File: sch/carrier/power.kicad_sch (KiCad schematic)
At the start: 0 parts

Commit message: noice.
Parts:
- added J1: 1054500101, MOLEXC:Molex-1054500101-MFG, symbol MOLEXC:1054500101
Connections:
- new net GND: J1.1 (MNT_1), J1.2 (MNT_2), J1.3 (MNT_3), J1.4 (MNT_4), J1.A1 (GND), J1.A12 (GND), J1.B1 (GND), J1.B12 (GND)

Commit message: goodnight
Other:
- title: (none) -> Power and battery
- moved on the sheet: J1A, J1B, J1C

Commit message: hhhhhhhhhhhhhhhhh
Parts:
- added D2: 5.1v, Diode_THT:D_DO-41_SOD81_P7.62mm_Horizontal, symbol Device:D_Zener
- added Q1, Q2: BC557, Package_TO_SOT_THT:TO-92_Inline, symbol Transistor_BJT:BC557
- added R14, R15: 5.1k, Resistor_SMD:R_0805_2012Metric_Pad1.20x1.40mm_HandSolder, symbol Device:R
- added R16: 2k, Resistor_SMD:R_0805_2012Metric_Pad1.20x1.40mm_HandSolder, symbol Device:R
- added R17: 1k, Resistor_SMD:R_0805_2012Metric_Pad1.20x1.40mm_HandSolder, symbol Device:R
- added R18: 6.2k, Resistor_SMD:R_0805_2012Metric_Pad1.20x1.40mm_HandSolder, symbol Device:R
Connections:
- net GND: now also D2.2 (A), R14.2, R15.2, R18.1
- net at J1.B4 (VBUS): now also J1.A4 (VBUS), J1.A9 (VBUS), J1.B9 (VBUS), Q1.1 (C), Q2.1 (C), R16.1
- net at J1.B5 (CC2): now also R15.1
- net at J1.A5 (CC1): now also R14.1
- new net: D2.1 (K), R16.2, R17.1
- new net: Q1.2 (B), R17.2
- new net: Q1.3 (E), Q2.2 (B), R18.2
- new net 5v: Q2.3 (E)
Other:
- note added: "5V 3A OUTPUT"
- note added: "5v overvolt prot - turns off >5.5v"

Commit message: put some stuff on the pcb - it is going to kill me trying to get all on
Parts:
- Q1, Q2: footprint Package_TO_SOT_THT:TO-92_Inline -> Package_TO_SOT_THT:TO-92_Inline_Horizontal1
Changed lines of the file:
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@@
-    (stroke (width 0) (type solid) (color 0 0 0 0))
-  )
-  (wire (pts (xy 66.675 142.875) (xy 85.725 142.875))
     (stroke (width 0) (type solid) (color 0 0 0 0))
   )
@@
     (effects (font (size 1.27 1.27)) (justify right bottom))
   )
-  (text "5v overvolt prot - turns off >5.5v\n" (at 96.52 107.315 180)
+  (text "5v overvolt prot - turns off >5.5v\n" (at 100.33 112.395 180)
     (effects (font (size 1.27 1.27)) (justify right bottom))
   )
-  (hierarchical_label "5v" (shape input) (at 107.95 139.065 0)
+  (hierarchical_label "5v" (shape output) (at 107.95 139.065 0)
     (effects (font (size 1.27 1.27)) (justify left))
   )
@@
     )
     (property "Datasheet" "" (id 3) (at 66.675 142.875 0)
+      (effects (font (size 1.27 1.27)) hide)
+    )
+    (pin "1")
+  )
+  (symbol (lib_id "power:GND") (at 85.725 142.875 0) (unit 1)
+    (in_bom yes) (on_board yes) (fields_autoplaced)
+    (property "Reference" "#PWR0101" (id 0) (at 85.725 149.225 0)
+      (effects (font (size 1.27 1.27)) hide)
+    )
+    (property "Value" "GND" (id 1) (at 85.725 147.32 0))
+    (property "Footprint" "" (id 2) (at 85.725 142.875 0)
+      (effects (font (size 1.27 1.27)) hide)
+    )
+    (property "Datasheet" "" (id 3) (at 85.725 142.875 0)
       (effects (font (size 1.27 1.27)) hide)
     )
@@
   )
   (symbol (lib_id "Device:D_Zener") (at 66.675 139.065 270) (unit 1)
-    (in_bom yes) (on_board yes) (fields_autoplaced)
+    (in_bom yes) (on_board yes)
     (property "Reference" "D2" (id 0) (at 69.215 137.7949 90)
       (effects (font (size 1.27 1.27)) (justify left))
@@
       (effects (font (size 1.27 1.27)) hide)
     )
-    (property "Model" "1N4733" (id 4) (at 66.675 139.065 90)
-      (effects (font (size 1.27 1.27)) hide)
-    )
+    (property "Model" "1N4733" (id 4) (at 61.595 139.065 90))
     (pin "1")
     (pin "2")
@@
       (effects (font (size 1.27 1.27)) (justify left))
     )
-    (property "Footprint" "Package_TO_SOT_THT:TO-92_Inline" (id 2) (at 88.265 129.54 0)
+    (property "Footprint" "Package_TO_SOT_THT:TO-92_Inline_Horizontal1" (id 2) (at 88.265 129.54 0)
       (effects (font (size 1.27 1.27) italic) (justify left) hide)
     )
@@
       (effects (font (size 1.27 1.27)) (justify left))
     )
-    (property "Footprint" "Package_TO_SOT_THT:TO-92_Inline" (id 2) (at 104.14 135.89 0)
+    (property "Footprint" "Package_TO_SOT_THT:TO-92_Inline_Horizontal1" (id 2) (at 104.14 135.89 0)
       (effects (font (size 1.27 1.27) italic) (justify left) hide)
     )
@@
   (symbol (lib_id "MOLEXC:1054500101") (at 28.575 52.705 0) (unit 1)
     (in_bom yes) (on_board yes)
-    (property "Reference" "J1" (id 0) (at 17.78 19.2405 90))
+    (property "Reference" "J1" (id 0) (at 19.05 42.7355 0))
     (property "Value" "1054500101" (id 1) (at 19.8755 44.45 0))
     (property "Footprint" "MOLEXC:Molex-1054500101-MFG" (id 2) (at 28.575 40.005 0)

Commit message: holy shit i hate chargers
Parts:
- added C? (x2): 4.7uF, symbol Device:C
- added C?: 10uF, symbol Device:C
- added R?: 110k, symbol Device:R
- added R?: 290k, symbol Device:R
- added U?: DS2745U, Package_SO:TSSOP-8_3x3mm_P0.65mm, symbol Battery_Management:DS2745U
- added U?: MCP73871-2CC, Package_DFN_QFN:QFN-20-1EP_4x4mm_P0.5mm_EP2.5x2.5mm, symbol Battery_Management:MCP73871-2CC
- added U?: MT3608, Package_TO_SOT_SMD:SOT-23-6, symbol Regulator_Switching:MT3608
- added U?: TPS61230DRC, Package_SON:Texas_S-PVSON-N10_ThermalVias, symbol Regulator_Switching:TPS61230DRC
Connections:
- net 5v: no longer Q2.3 (E)
- net GND: now also J1.A1 (GND), J1.A1 (GND), J1.A12 (GND), J1.A2 (TX1+), J1.A3 (TX1-), J1.A4 (VBUS), C?.2, C?.2, R?.2, U?.10 (VSS), U?.11 (VSS), U?.21 (VSS); no longer J1.1 (MNT_1), J1.2 (MNT_2), J1.3 (MNT_3), J1.4 (MNT_4), J1.B1 (GND), J1.B12 (GND)
- net at R15.1: now also J1.A5 (CC1); no longer J1.B5 (CC2)
- net at Q2.2 (B), R18.2: now also Q1.1 (C); no longer Q1.3 (E)
- new net: J1.A4 (VBUS), J1.A4 (VBUS), J1.A9 (VBUS), J1.A9 (VBUS), Q1.3 (E), Q2.3 (E), R16.1
- new net: R?.1, R?.2, U?.2 (VPCC)
- new net: C?.1, U?.14 (VBAT), U?.15 (VBAT), U?.16 (Vbat_SENSE)
- new net: C?.1, U?.1 (OUT), U?.20 (OUT)
- new net: U?.1 (SW), U?.2 (SW)
- new net: U?.3 (VOUT), U?.4 (VOUT)
- new net VUSB: C?.1, Q2.1 (C), R?.1, U?.18 (IN), U?.19 (IN)
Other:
- note added: "battery monitor board"

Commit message: h
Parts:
- removed C? (x2): 4.7uF, symbol Device:C
- removed C?: 10uF, symbol Device:C
- removed J1 (x3): 1054500101, MOLEXC:Molex-1054500101-MFG, symbol MOLEXC:1054500101
- removed R14, R15: 5.1k, Resistor_SMD:R_0805_2012Metric_Pad1.20x1.40mm_HandSolder, symbol Device:R
- removed R?: 110k, symbol Device:R
- removed R?: 290k, symbol Device:R
- removed U?: DS2745U, Package_SO:TSSOP-8_3x3mm_P0.65mm, symbol Battery_Management:DS2745U
- removed U?: MCP73871-2CC, Package_DFN_QFN:QFN-20-1EP_4x4mm_P0.5mm_EP2.5x2.5mm, symbol Battery_Management:MCP73871-2CC
- removed U?: MT3608, Package_TO_SOT_SMD:SOT-23-6, symbol Regulator_Switching:MT3608
- added C? (x5): C, symbol Device:C
- added D? (x2): LED, symbol Device:LED
- added J4: USB_C_Receptacle_USB2.0, Connector_USB:USB_C_Receptacle_JAE_DX07S016JA1R1500, symbol Connector:USB_C_Receptacle_USB2.0
- added L?: L, symbol Device:L
- added R20, R21: 5.1k, Resistor_SMD:R_0805_2012Metric_Pad1.20x1.40mm_HandSolder, symbol Device:R
- added R? (x8): R, symbol Device:R
- added R?: 0, symbol Device:R
- added U?: MP2617BGL-P, symbol MP:MP2617BGL-P
- gave numbers to parts that had none: 1
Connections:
- net GND: now also C?.1, C?.1, C?.2, J4.A1 (GND), J4.A12 (GND), J4.B1 (GND), J4.B12 (GND), R20.2, R21.2, R?.2, R?.2, R?.2, R?.2, U?.5 (PGND)
- new net: C?.2, L?.1, U?.13 (SYS)
- new net: J4.A5 (CC1), R20.1
- new net: D?.1 (K), U?.10 (*ACOK)
- new net: D?.2 (A), R?.1 (x2)
- new net: J4.B5 (CC2), R21.1
- new net: J4.S1 (SHIELD), R?.1
- new net: C?.2, R?.1
- new net: R?.1, U?.17 (ILIM)
- new net: R?.1, R?.2, U?.16 (NTC)
- new net: D?.1 (K), U?.9 (*CHGOK)
- new net: R?.1, U?.15 (ISET)
- new net: C?.1, L?.2, U?.2 (SW), U?.4 (SW)
- new net: C?.2, U?.1 (BST)
- new net: C?.2, U?.18 (TMR)
- new net BATT_CHRG: U?.14 (BATT)
- new net MP2617__vcc: R?.1, R?.1, R?.2, R?.2, R?.2, U?.19 (VLIM), U?.20 (VCC)
- new net VBUS: C?.1, J4.A4 (VBUS), J4.A9 (VBUS), J4.B4 (VBUS), J4.B9 (VBUS), R?.2
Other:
- note added: "Based off MP2617 datasheet. TODO: make the values do things."
- note added: "Too many people on stack overflow/exchange seem to be unable to agree on this! Leaving this unconnected with a 0 ohm so we can if we choose to."
- note added: "battery monitor board we will write software for this, but it is not intially required"
- note removed: "battery monitor board"
- moved on the sheet: D2, Q1, Q2, R16, R17, R18, U5

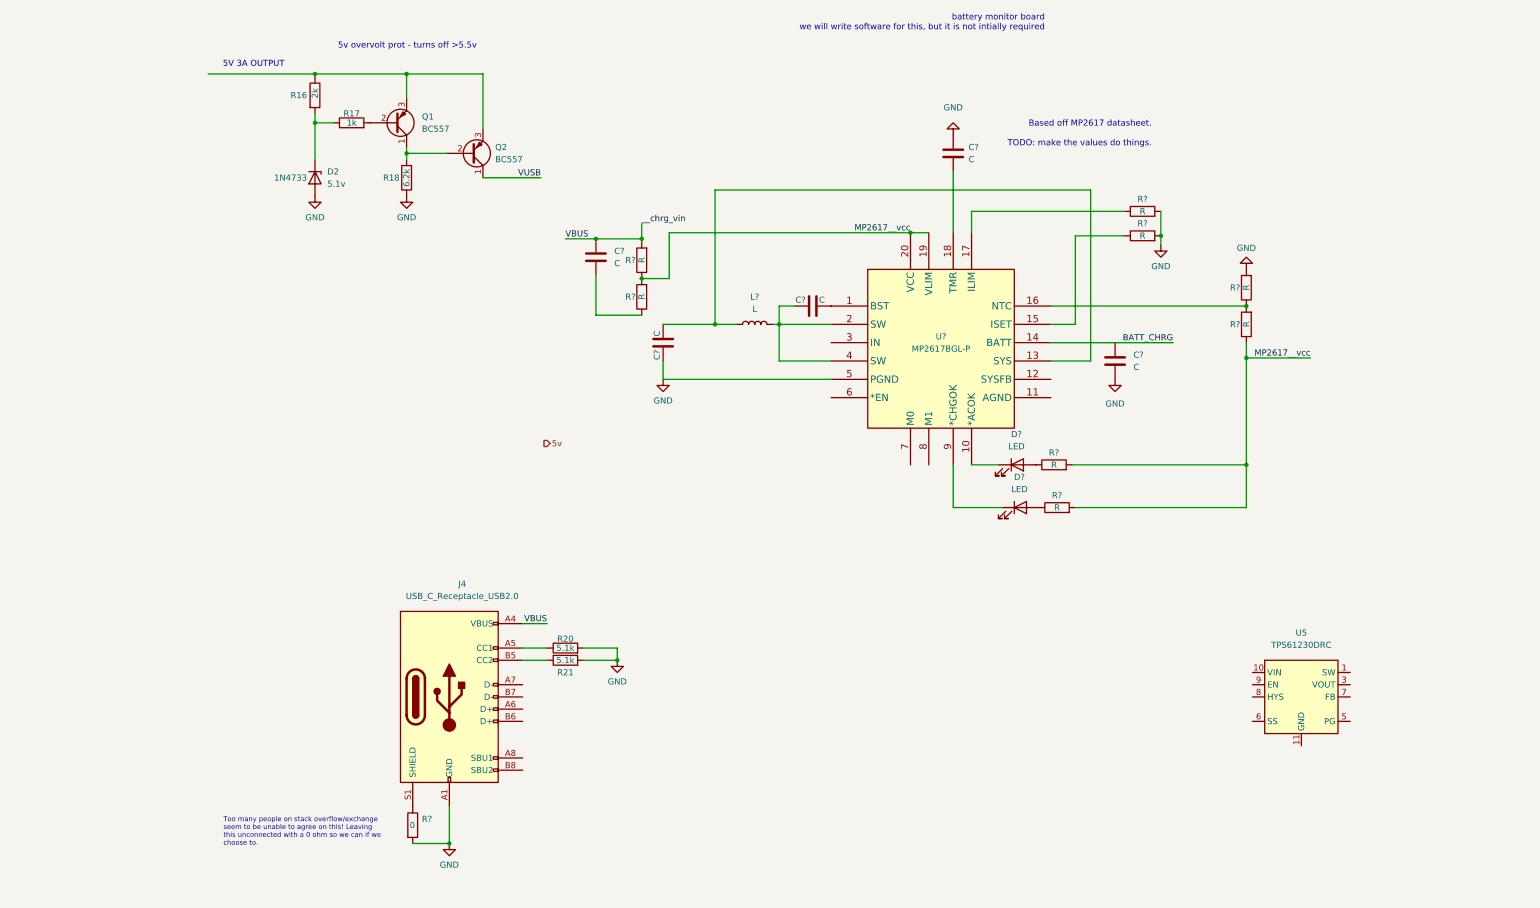
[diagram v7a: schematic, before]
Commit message: bring in line with the datasheet
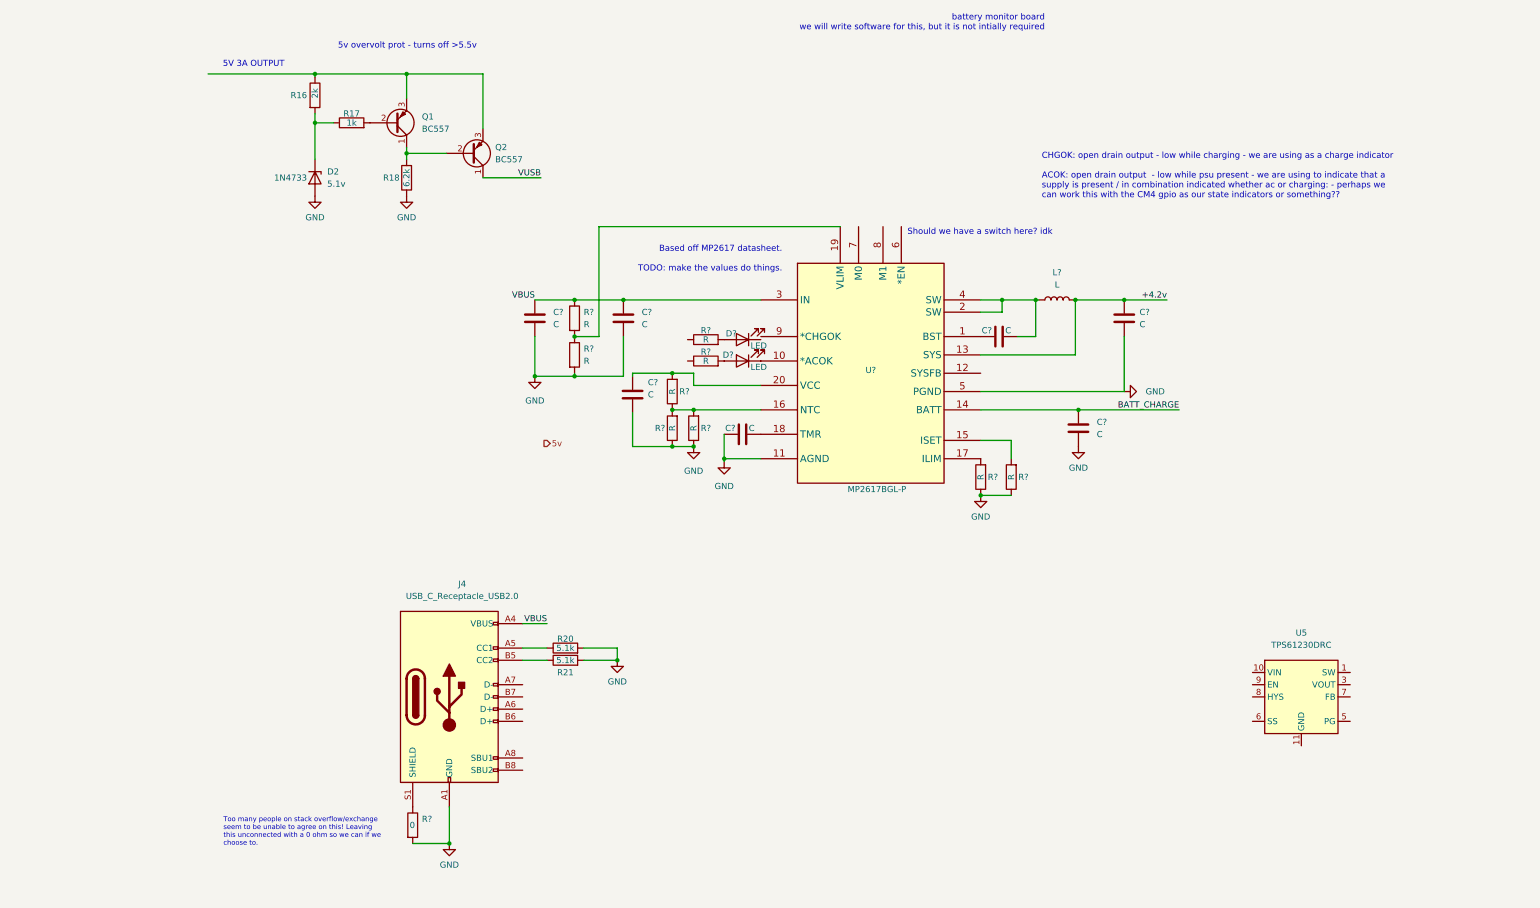
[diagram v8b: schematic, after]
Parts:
- removed C? (x5): C, symbol Device:C
- removed D? (x2): LED, symbol Device:LED
- removed L?: L, symbol Device:L
- removed R? (x8): R, symbol Device:R
- added C? (x7): C, symbol Device:C
- added D? (x2): LED, symbol Device:LED
- added L?: L, symbol Device:L
- added R? (x9): R, symbol Device:R
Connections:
- net GND: now also U?.11 (AGND), C?.1, C?.2, C?.2, C?.2, C?.2, C?.2, R?.1, R?.1, R?.1, R?.1, R?.2
- net VBUS: now also U?.3 (IN), C?.1, C?.1, R?.1
- net +4.2v: now reaches U?.13 (SYS)
- net +4.2v: now also C?.1, L?.2
- net at U?.10 (*ACOK): now also D?.1 (K)
- net at U?.17 (ILIM): now also R?.2
- net at U?.16 (NTC): now also R?.1, R?.2, R?.2
- net at U?.15 (ISET): now also R?.2
- net at U?.2 (SW), U?.4 (SW): now also C?.2, L?.1
- net at U?.1 (BST): now also C?.1
- net at U?.18 (TMR): now also C?.2
- net BATT_CHRG renamed BATT_CHARGE
- net BATT_CHARGE: now also C?.1
- net MP2617__vcc: no longer names the net of U?.20 (VCC)
- net MP2617__vcc: now also C?.1, R?.2; no longer U?.19 (VLIM)
- new net: D?.2 (A), R?.2 (x2)
- new net: R?.1, R?.2, U?.19 (VLIM)
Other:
- note added: "CHGOK: open drain output - low while charging - we are using as a charge indicator ACOK: open drain output - low while psu present - we are using to indicate that a supply is present / in combination indicated whether ac or charging: - perhaps we can work this with the CM4 gpio as our state indicators or something??"
- note added: "Should we have a switch here? idk"
- moved on the sheet: U?
